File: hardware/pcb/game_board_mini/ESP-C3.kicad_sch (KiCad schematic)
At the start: 25 parts, among them J6 USB_C_Receptacle, SW1 SW_Push, U1 ESP32-C3, U2 USBLC6-2SC6, Y1 Crystal_GND24

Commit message: [PCB] Routed ESP
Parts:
- C73, C74, C75, C76, C77, C81, C82: footprint Capacitor_SMD:C_0805_2012Metric -> Capacitor_SMD:C_0603_1608Metric
- C78: value 1µF -> 1µ; footprint Capacitor_SMD:C_0805_2012Metric -> Capacitor_SMD:C_0603_1608Metric
- C79, C80: value 10µF -> 10µ; footprint Capacitor_SMD:C_0805_2012Metric -> Capacitor_SMD:C_0603_1608Metric
- C83, C84: value 0.1µF -> 100n; footprint Capacitor_SMD:C_0805_2012Metric -> Capacitor_SMD:C_0603_1608Metric
- L1, L2: footprint Inductor_SMD:L_0805_2012Metric -> Inductor_SMD:L_0603_1608Metric
- R77, R78, R79, R80: footprint Resistor_SMD:R_0805_2012Metric -> Resistor_SMD:R_0603_1608Metric
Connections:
- net GND: no longer AE1.1 (FEED)
- new net ANT_PAD1: AE1.1 (FEED)
- no-connect marks 17 -> 18

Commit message: [PCB] Increased board size
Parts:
- R76: footprint Resistor_SMD:R_0805_2012Metric -> Resistor_SMD:R_0603_1608Metric
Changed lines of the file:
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@@
       (effects (font (size 1.27 1.27)) (justify left))
     )
-    (property "Footprint" "Resistor_SMD:R_0805_2012Metric" (id 2) (at 261.112 29.21 90)
+    (property "Footprint" "Resistor_SMD:R_0603_1608Metric" (id 2) (at 261.112 29.21 90)
       (effects (font (size 1.27 1.27)) hide)
     )

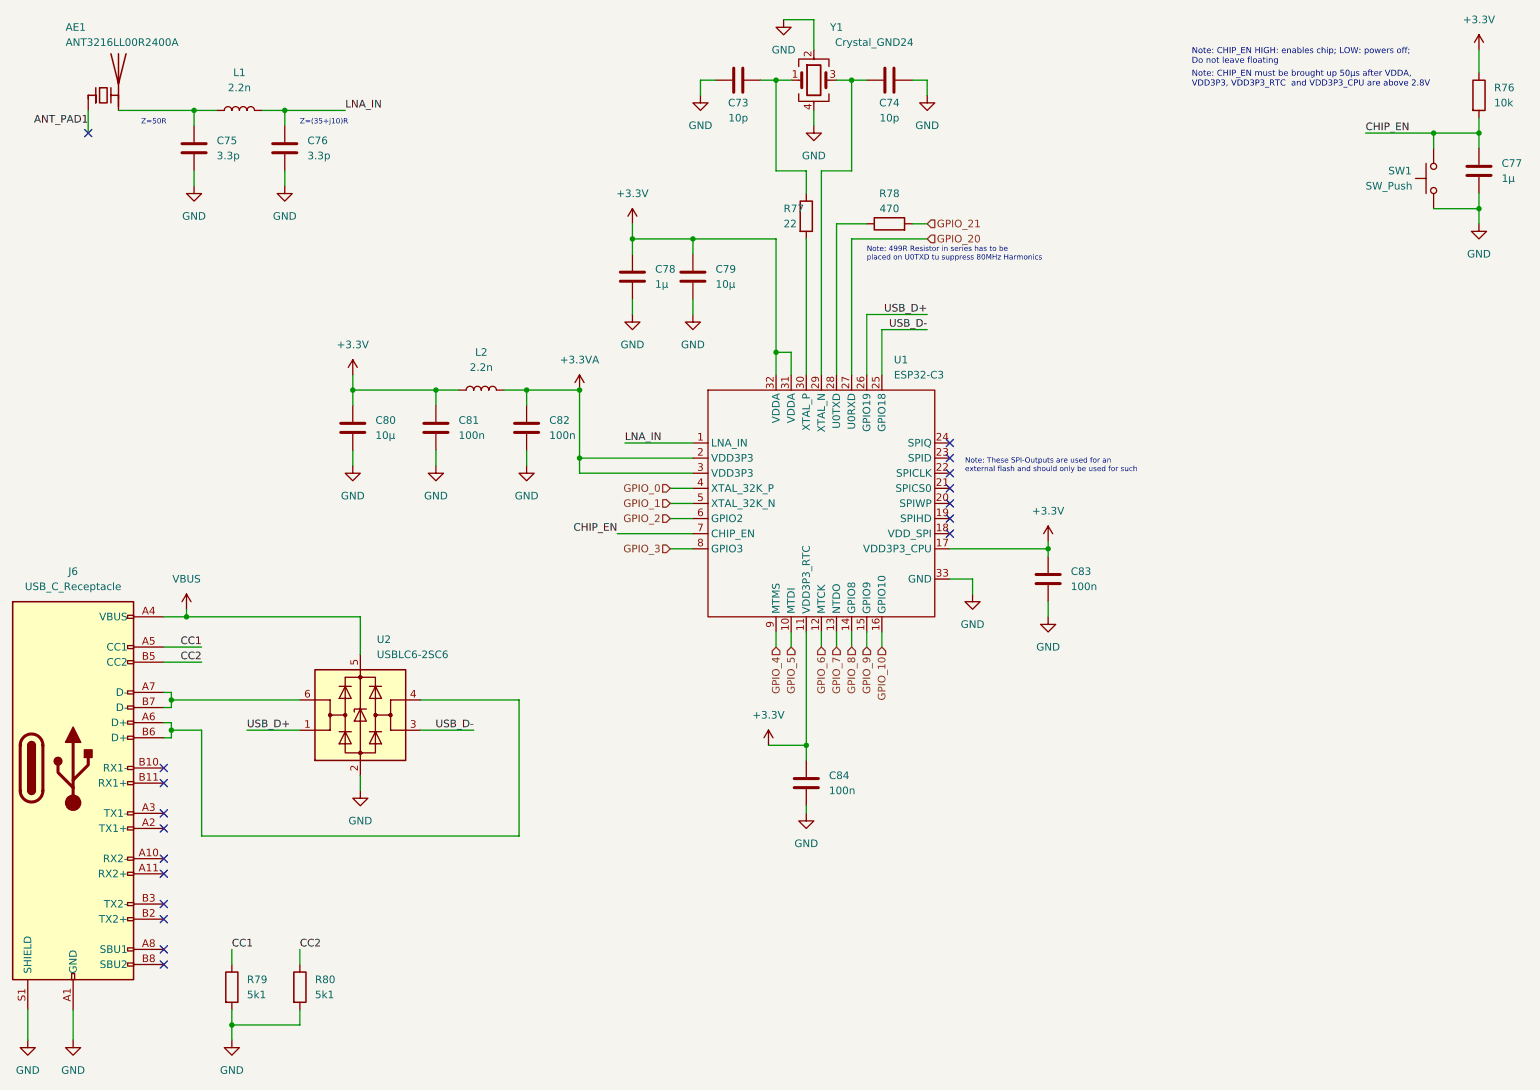
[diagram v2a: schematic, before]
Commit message: Fixed bug: `player_count` and `brightness` reset in loop
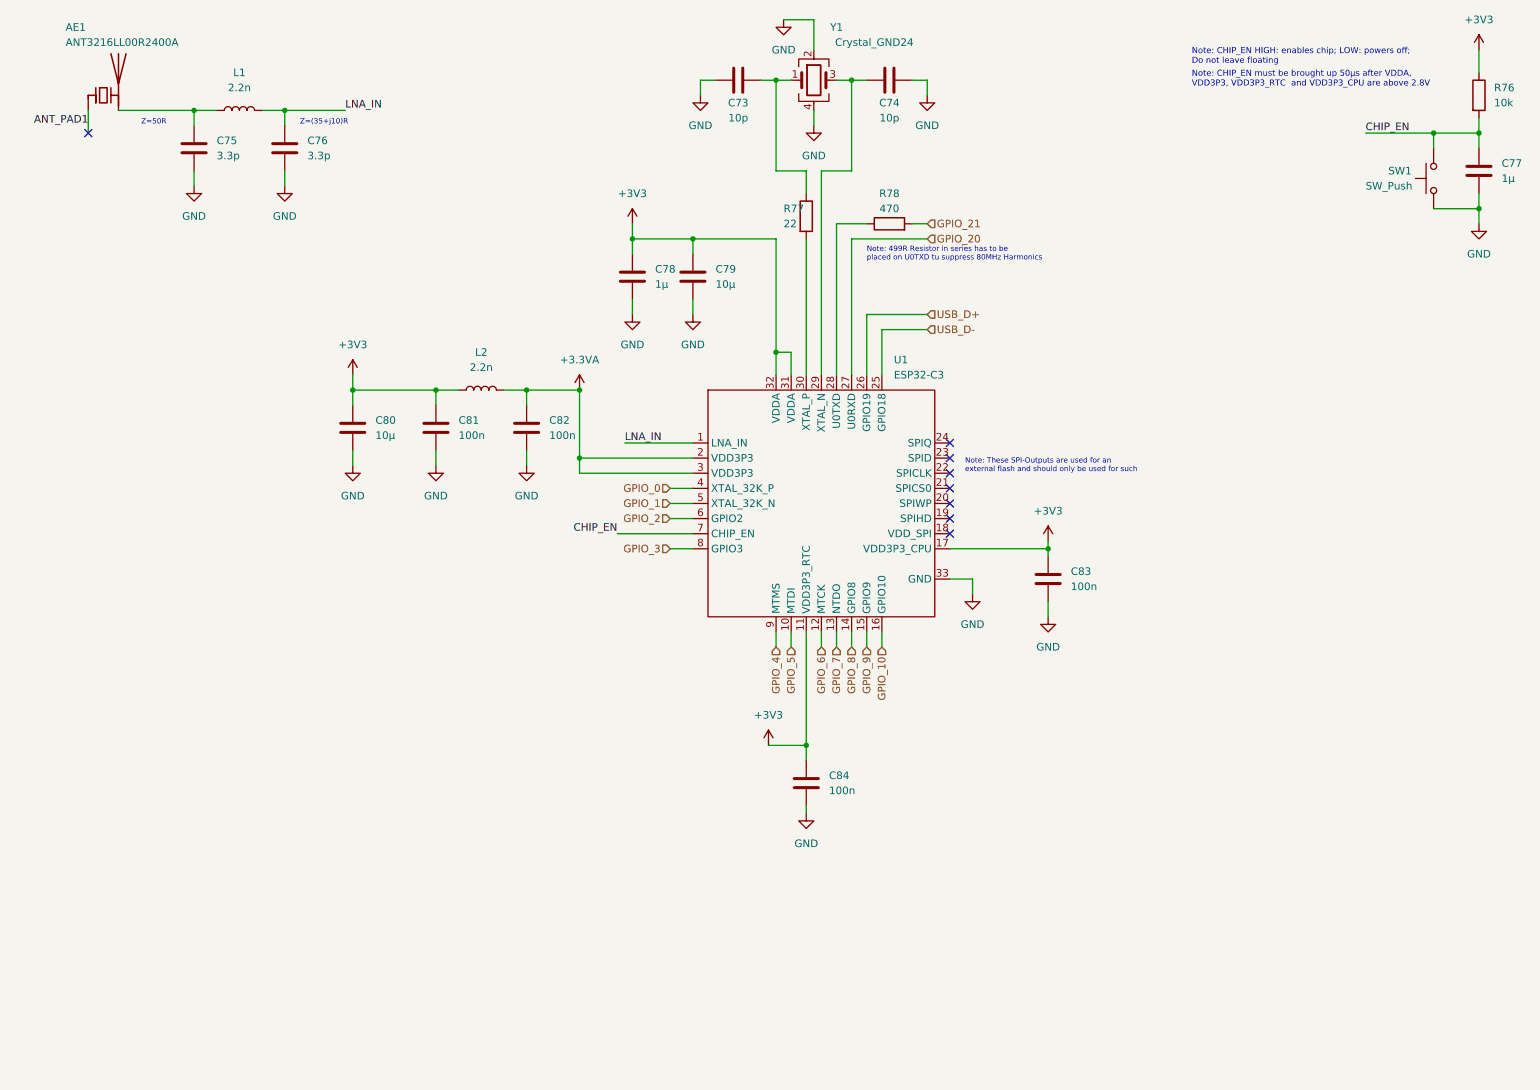
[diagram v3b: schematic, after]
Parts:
- removed J6: USB_C_Receptacle, USB_C:USB_C_MOLEX_1054500101, symbol Connector:USB_C_Receptacle
- removed R79, R80: 5k1, Resistor_SMD:R_0603_1608Metric, symbol Device:R
- removed U2: USBLC6-2SC6, Package_TO_SOT_SMD:SOT-23-6, symbol Power_Protection:USBLC6-2SC6
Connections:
- net +3.3V renamed +3V3
- no-connect marks 18 -> 8
